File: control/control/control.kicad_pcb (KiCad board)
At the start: 2 copper layers, 101.6 x 101.6 mm, 82 parts, among them J1 Molex2x15, Q1 2N3904, Q2 2N3904, Q3 2N3904, SW2 SW_SPST, U1 LM3914N

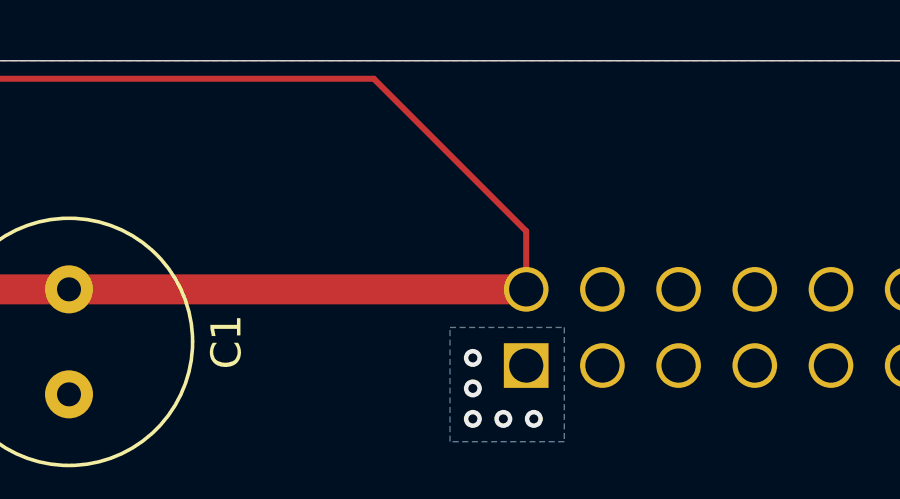
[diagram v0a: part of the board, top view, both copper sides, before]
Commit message: add joystick plug, adjust resistors
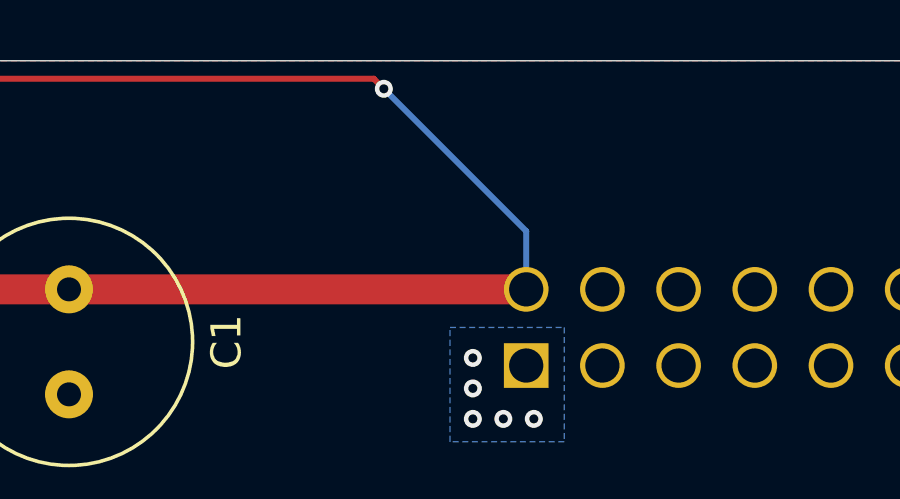
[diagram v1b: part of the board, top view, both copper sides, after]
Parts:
- R13, R14, R15, R16, R17, R18, R19, R20, R21, R22, R23, R24, R25, R26, R27, R28, R29, R30, R31, R32, R33, R34, R35, R36, R37, R38, R39, R40, R41, R42, R43, R44, R45, R46, R47, R48, R49, R50, R51, R52, R53, R54, R55, R56, R57, R58, R59, R60, R61, R62: value 1k -> 18k
- U2: value ~ -> 3.3v regulator
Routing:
- net vbat: vias 0 -> 1
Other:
- board text added: "18k"
- board text removed: "1k"

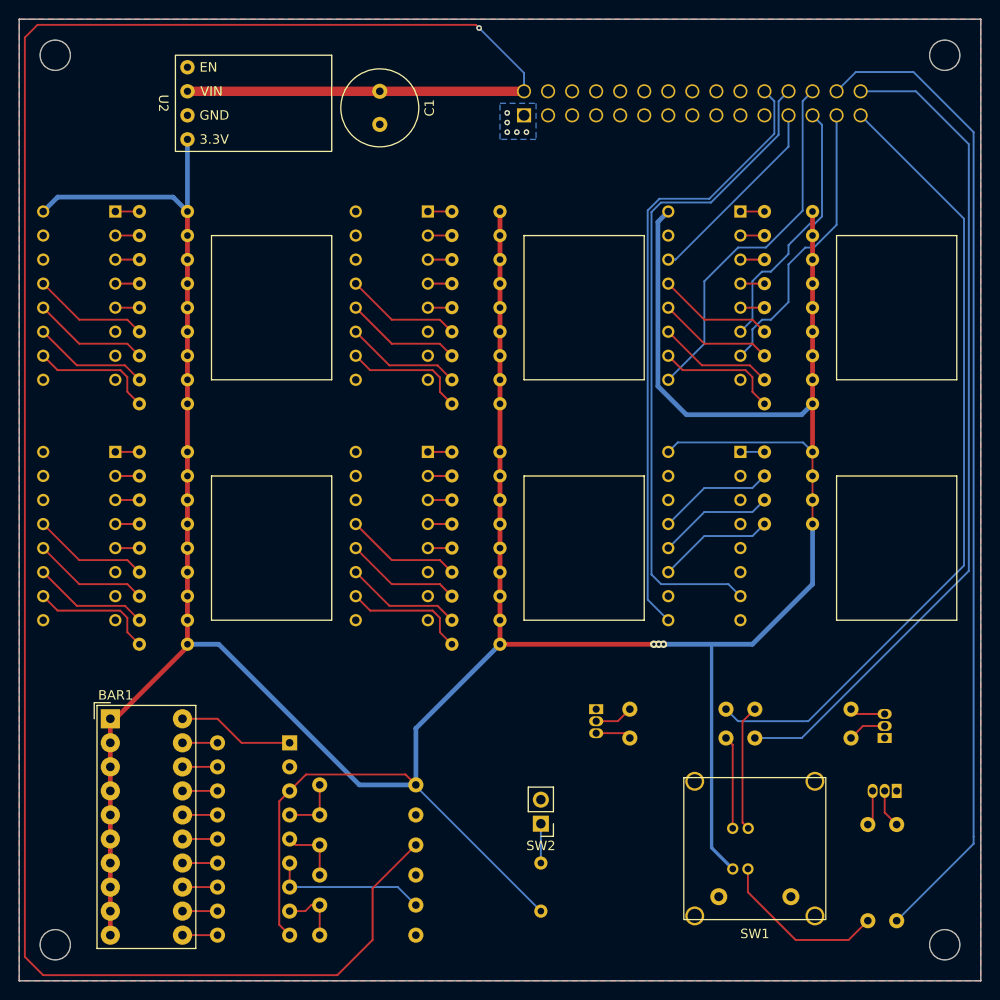
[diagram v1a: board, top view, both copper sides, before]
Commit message: delete binary converter chips and add different knobs
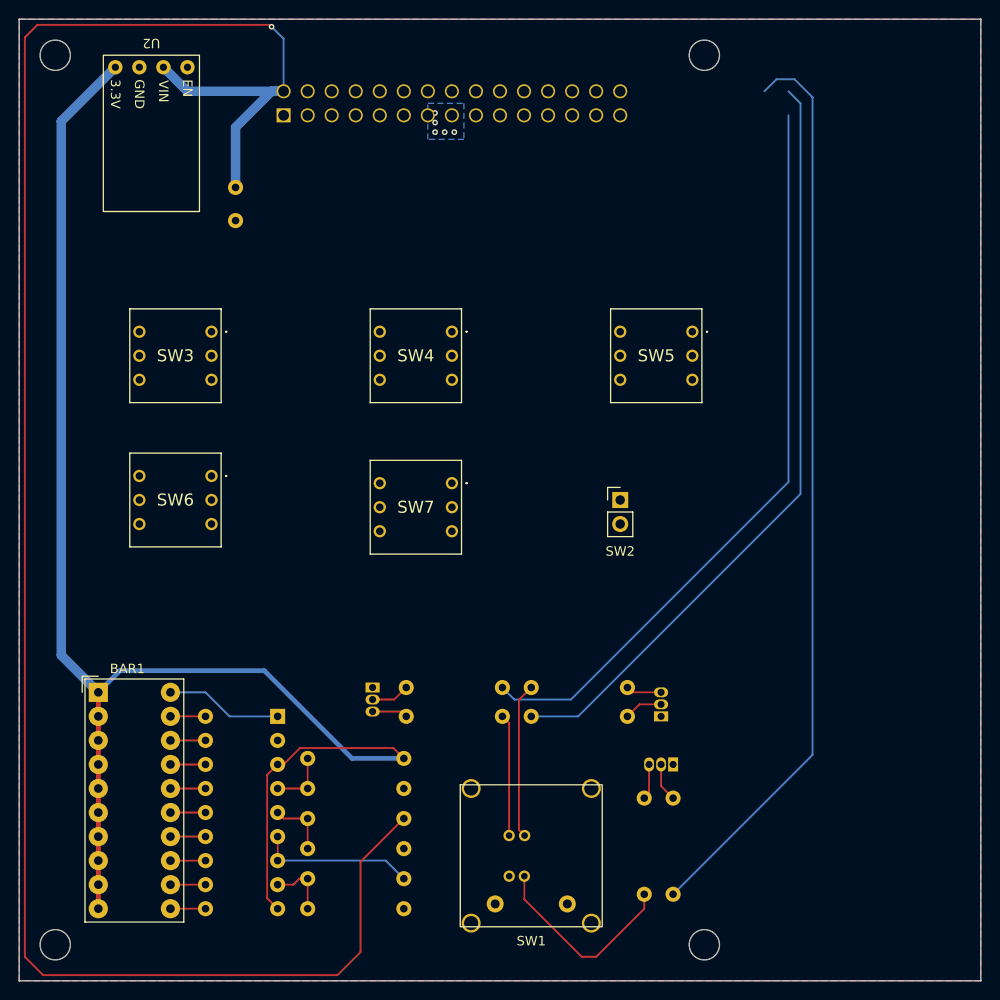
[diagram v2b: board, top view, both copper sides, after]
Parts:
- removed E1, E2, E3, E4, E5, E6: CD74HC147E, projlib:CD74HC147E
- removed R13, R14, R15, R16, R17, R18, R19, R20, R21, R22, R23, R24, R25, R26, R27, R28, R29, R30, R31, R32, R33, R34, R35, R36, R37, R38, R39, R40, R41, R42, R43, R44, R45, R46, R47, R48, R49, R50, R51, R52, R53, R54, R55, R56, R57, R58, R59, R60, R61, R62: 18k, Resistor_THT:R_Axial_DIN0204_L3.6mm_D1.6mm_P5.08mm_Horizontal
- added SW3: 221AMC10R, projlib:221ADC16, F.Cu at (121.9, 83.8)
- added SW4: 221AMC10R, projlib:221ADC16, F.Cu at (147.3, 83.8)
- added SW5: 221AMC10R, projlib:221ADC16, F.Cu at (172.7, 83.8)
- added SW6: 221AMC10R, projlib:221ADC16, F.Cu at (121.9, 99.1)
- added SW7: 221AMC10R, projlib:221ADC16, F.Cu at (147.3, 99.8)
- C1: moved to B.Cu
- moved SW2 35.2 mm to (165.1, 101.6), turned to 0 degrees
- moved J1 25.4 mm to (129.5, 61.0)
- moved REF** 25.4 mm to (174.0, 54.6)
- moved REF** 25.4 mm to (174.0, 148.6)
- moved Q3 23.8 mm to (170.7, 129.5)
- moved R11 23.8 mm to (170.7, 133.1)
- moved R12 23.8 mm to (167.6, 133.1)
- moved R10 23.7 mm to (142.5, 124.5)
- moved R7 23.7 mm to (165.9, 124.5)
- moved Q2 23.7 mm to (138.9, 121.4)
- moved R8 23.7 mm to (165.9, 121.4)
- moved R9 23.7 mm to (142.5, 121.4)
- moved Q1 23.7 mm to (169.4, 124.5)
- moved SW1 23.6 mm to (155.7, 139.2)
- moved C1 18.3 mm to (124.5, 68.6)
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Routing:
- net 3.3V: track 401.0 -> 161.1 mm, vias 3 -> 0
- net enc6_1: track 70.5 -> 0.00 mm
- net enc6_0: track 65.8 -> 0.00 mm
- net enc3_0: track 38.5 -> 0.00 mm
- net enc3_1: track 30.7 -> 0.00 mm
- net vbat: track 241.0 -> 211.2 mm
- net enc3_2: track 27.7 -> 0.00 mm
- net enc3_3: track 21.5 -> 0.00 mm
- net Net-(E3-*I9): track 13.2 -> 0.00 mm
- net Net-(E1-*I9): track 13.2 -> 0.00 mm
- net Net-(E2-*I9): track 13.2 -> 0.00 mm
- net Net-(E5-*I9): track 13.2 -> 0.00 mm
- net Net-(E4-*I9): track 13.2 -> 0.00 mm
- net Net-(E3-*I1): track 12.3 -> 0.00 mm
- net Net-(E1-*I1): track 12.3 -> 0.00 mm
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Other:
- board text removed: "18k"

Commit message: control pcb almost done
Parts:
- removed SW2: SW_SPST, Connector_PinHeader_2.54mm:PinHeader_1x02_P2.54mm_Vertical
- added R13: 2k, Resistor_THT:R_Axial_DIN0207_L6.3mm_D2.5mm_P10.16mm_Horizontal, B.Cu at (146.1, 115.6)
- added REF**: TestPoint_Pad_D1.0mm, TestPoint:TestPoint_Pad_D1.0mm, F.Cu at (174.8, 61.5)
- added S1: LP4EE1PBCTW, projlib:LP4EE1PBCTW, F.Cu at (165.1, 79.5)
- added U3: ~, projlib:R20405RN02Q, F.Cu at (158.8, 105.4)
- Q1, Q2, Q3: footprint Package_TO_SOT_THT:TO-92_Inline -> projlib:TO-92_Inline
- SW3, SW4, SW5, SW6, SW7: value 221AMC10R -> 221ADC16
- moved SW5 18.9 mm to (154.3, 79.4)
- moved SW4 11.7 mm to (136.5, 79.4)
- moved SW7 10.9 mm to (136.5, 101.1)
- moved SW3 5.46 mm to (118.7, 79.4)
- moved SW6 3.77 mm to (118.7, 101.1)
- moved C1 2.01 mm to (125.1, 70.5), turned to 0 degrees
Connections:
- J1 pad 10: unconnected-(J1-Pin_10-Pad10) -> Net-(J1-Pin_10)
- J1 pad 11: unconnected-(J1-Pin_11-Pad11) -> Net-(J1-Pin_11)
- J1 pad 12: unconnected-(J1-Pin_12-Pad12) -> Net-(J1-Pin_12)
- J1 pad 13: unconnected-(J1-Pin_13-Pad13) -> Net-(J1-Pin_13)
- J1 pad 14: unconnected-(J1-Pin_14-Pad14) -> Net-(J1-Pin_14)
- J1 pad 15: unconnected-(J1-Pin_15-Pad15) -> Net-(J1-Pin_15)
- J1 pad 16: unconnected-(J1-Pin_16-Pad16) -> Net-(J1-Pin_16)
- J1 pad 17: unconnected-(J1-Pin_17-Pad17) -> Net-(J1-Pin_17)
- J1 pad 18: unconnected-(J1-Pin_18-Pad18) -> Net-(J1-Pin_18)
- J1 pad 19: unconnected-(J1-Pin_19-Pad19) -> Net-(J1-Pin_19)
- J1 pad 20: unconnected-(J1-Pin_20-Pad20) -> Net-(J1-Pin_20)
- J1 pad 21: unconnected-(J1-Pin_21-Pad21) -> Net-(J1-Pin_21)
- J1 pad 22: enc6_0 -> Net-(J1-Pin_22)
- J1 pad 23: enc3_3 -> mode2
- J1 pad 24: enc6_1 -> mode1
- J1 pad 25: enc3_2 -> activate
- J1 pad 26: enc3_0 -> Net-(J1-Pin_26)
- J1 pad 27: enc3_1 -> steerlock
- J1 pad 3: unconnected-(J1-Pin_3-Pad3) -> Net-(J1-Pin_3)
- J1 pad 4: unconnected-(J1-Pin_4-Pad4) -> Net-(J1-Pin_4)
- J1 pad 5: unconnected-(J1-Pin_5-Pad5) -> Net-(J1-Pin_5)
- J1 pad 6: unconnected-(J1-Pin_6-Pad6) -> Net-(J1-Pin_6)
- J1 pad 7: unconnected-(J1-Pin_7-Pad7) -> Net-(J1-Pin_7)
- J1 pad 8: unconnected-(J1-Pin_8-Pad8) -> Net-(J1-Pin_8)
- J1 pad 9: unconnected-(J1-Pin_9-Pad9) -> Net-(J1-Pin_9)
- R3 pad 1: vbat -> Net-(J1-Pin_26)
- SW3 pad 1: unconnected-(SW3-8-Pad1) -> Net-(J1-Pin_6)
- SW3 pad 2: unconnected-(SW3-4-Pad2) -> Net-(J1-Pin_8)
- SW3 pad 4: unconnected-(SW3-2-Pad4) -> Net-(J1-Pin_4)
- SW3 pad 8: unconnected-(SW3-1-Pad8) -> Net-(J1-Pin_10)
- SW4 pad 1: unconnected-(SW4-8-Pad1) -> Net-(J1-Pin_14)
- SW4 pad 2: unconnected-(SW4-4-Pad2) -> Net-(J1-Pin_11)
- SW4 pad 4: unconnected-(SW4-2-Pad4) -> Net-(J1-Pin_13)
- SW4 pad 8: unconnected-(SW4-1-Pad8) -> Net-(J1-Pin_12)
- SW5 pad 1: unconnected-(SW5-8-Pad1) -> Net-(J1-Pin_22)
- SW5 pad 2: unconnected-(SW5-4-Pad2) -> Net-(J1-Pin_19)
- SW5 pad 4: unconnected-(SW5-2-Pad4) -> Net-(J1-Pin_21)
- SW5 pad 8: unconnected-(SW5-1-Pad8) -> Net-(J1-Pin_20)
- SW6 pad 1: unconnected-(SW6-8-Pad1) -> Net-(J1-Pin_7)
- SW6 pad 2: unconnected-(SW6-4-Pad2) -> Net-(J1-Pin_5)
- SW6 pad 4: unconnected-(SW6-2-Pad4) -> Net-(J1-Pin_9)
- SW6 pad 8: unconnected-(SW6-1-Pad8) -> Net-(J1-Pin_3)
- SW7 pad 1: unconnected-(SW7-8-Pad1) -> Net-(J1-Pin_18)
- SW7 pad 2: unconnected-(SW7-4-Pad2) -> Net-(J1-Pin_15)
- SW7 pad 4: unconnected-(SW7-2-Pad4) -> Net-(J1-Pin_17)
- SW7 pad 8: unconnected-(SW7-1-Pad8) -> Net-(J1-Pin_16)
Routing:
- net vbat: track 211.2 -> 28.8 mm, vias 1 -> 0
- net Net-(J1-Pin_26): track 0.00 -> 167.4 mm
- net activate: track 0.00 -> 106.3 mm
- net 3.3V: track 161.1 -> 263.8 mm
- net mode2: track 0.00 -> 67.5 mm
- net Net-(J1-Pin_5): track 0.00 -> 54.9 mm
- net Net-(J1-Pin_9): track 0.00 -> 53.9 mm
- net Net-(J1-Pin_15): track 0.00 -> 52.8 mm
- net Net-(J1-Pin_17): track 0.00 -> 50.7 mm
- net Net-(J1-Pin_16): track 0.00 -> 50.3 mm
- net Net-(J1-Pin_3): track 0.00 -> 49.9 mm
- net Net-(J1-Pin_18): track 0.00 -> 48.2 mm
- net Net-(J1-Pin_7): track 0.00 -> 47.8 mm
- net Net-(J1-Pin_8): track 0.00 -> 45.5 mm, vias 0 -> 1
- net mode1: track 0.00 -> 44.9 mm
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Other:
- board size 101.6 x 101.6 mm -> 76.2 x 101.6 mm
- board text added: "*"
- board text added: "1"
- board text added: "4"
- board text added: "8"
- board text added: "WayWayWay"

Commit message: final adjustments for v1.0
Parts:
- removed the REF** at (174.8, 61.5)
- added G***: LOGO, LOGO, F.Cu at (167.9, 68.8)
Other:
- board text added: "https://github.com/PNW-AT/standing-frame"
